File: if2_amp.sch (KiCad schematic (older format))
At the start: 0 parts

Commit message: if2_amp updated
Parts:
- added R? (x2): R, symbol Device:R
- added R? (x2): 100k, symbol Device:R
- added U?: MCP6D11, Package_SO:MSOP-8_3x3mm_P0.65mm, symbol sdr:MCP6D11
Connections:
- new net +5VA: R?.1, U?.3 (V+), U?.7 (/PD)
- new net 2.5V: R?.1, R?.2, U?.2 (Vocm)
- new net GND: R?.2, U?.6 (V-)
- new net In+: R?.2, U?.8 (+)
- new net In-: R?.2, U?.1 (-)
- new net Out+: R?.1, U?.4 (Out+)
- new net Out-: R?.1, U?.5 (Out-)
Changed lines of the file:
@@
 $Descr A4 11693 8268
 encoding utf-8
-Sheet 8 7
+Sheet 6 7
 Title ""
 Date ""
@@
 Comment4 ""
 $EndDescr
+$Comp
+L sdr:MCP6D11 U?
+U 1 1 5FEA4D4E
+P 2450 3150
+F 0 "U?" H 2400 4250 50  0000 C CNN
+F 1 "MCP6D11" H 2400 4150 50  0000 C CNN
+F 2 "Package_SO:MSOP-8_3x3mm_P0.65mm" H 2400 3000 50  0001 L CNN
+F 3 "http://www.ti.com/lit/ds/symlink/opa333.pdf" H 2850 3300 50  0001 C CNN
+	1    2450 3150
+	1    0    0    -1
+$EndComp
+Text HLabel 1800 3050 0    50   Input ~ 0
+In+
+Text HLabel 1800 3250 0    50   Input ~ 0
+In-
+Wire Wire Line
+	1800 3050 2050 3050
+Wire Wire Line
+	1800 3250 2050 3250
+Wire Wire Line
+	2500 2850 2400 2850
+$Comp
+L power:GND #PWR?
+U 1 1 5FEAC1C0
+P 2400 3450
+F 0 "#PWR?" H 2400 3200 50  0001 C CNN
+F 1 "GND" H 2400 3300 50  0000 C CNN
+F 2 "" H 2400 3450 50  0001 C CNN
+F 3 "" H 2400 3450 50  0001 C CNN
+	1    2400 3450
+	1    0    0    -1
+$EndComp
+$Comp
+L Device:R R?
+U 1 1 5FEAD645
+P 2400 2450
+F 0 "R?" V 2193 2450 50  0000 C CNN
+F 1 "R" V 2284 2450 50  0000 C CNN
+F 2 "" V 2330 2450 50  0001 C CNN
+F 3 "~" H 2400 2450 50  0001 C CNN
+	1    2400 2450
+	0    1    1    0
+$EndComp
+$Comp
+L Device:R R?
+U 1 1 5FEAE12B
+P 2400 3850
+F 0 "R?" V 2600 3850 50  0000 C CNN
+F 1 "R" V 2500 3850 50  0000 C CNN
+F 2 "" V 2330 3850 50  0001 C CNN
+F 3 "~" H 2400 3850 50  0001 C CNN
+	1    2400 3850
+	0    1    1    0
+$EndComp
+Wire Wire Line
+	2250 2450 2050 2450
+Wire Wire Line
+	2050 2450 2050 3050
+Connection ~ 2050 3050
+Wire Wire Line
+	2050 3050 2150 3050
+Wire Wire Line
+	2050 3250 2050 3850
+Wire Wire Line
+	2050 3850 2250 3850
+Connection ~ 2050 3250
+Wire Wire Line
+	2050 3250 2150 3250
+Wire Wire Line
+	2550 3850 2800 3850
+Wire Wire Line
+	2800 3850 2800 3250
+Wire Wire Line
+	2800 3050 2800 2450
+Wire Wire Line
+	2800 2450 2550 2450
+Text HLabel 3150 3050 2    50   Input ~ 0
+Out+
+Text HLabel 3150 3250 2    50   Input ~ 0
+Out-
+Wire Wire Line
+	3150 3050 2800 3050
+Connection ~ 2800 3050
+Wire Wire Line
+	2800 3250 3150 3250
+Connection ~ 2800 3250
+Wire Wire Line
+	2800 3150 2750 3150
+$Comp
+L power:+5VA #PWR?
+U 1 1 5FEB0DF4
+P 2400 2850
+F 0 "#PWR?" H 2400 2700 50  0001 C CNN
+F 1 "+5VA" H 2415 3023 50  0000 C CNN
+F 2 "" H 2400 2850 50  0001 C CNN
+F 3 "" H 2400 2850 50  0001 C CNN
+	1    2400 2850
+	1    0    0    -1
+$EndComp
+Connection ~ 2400 2850
+$Comp
+L power:+5VA #PWR?
+U 1 1 5FEB1889
+P 4000 2200
+F 0 "#PWR?" H 4000 2050 50  0001 C CNN
+F 1 "+5VA" H 4015 2373 50  0000 C CNN
+F 2 "" H 4000 2200 50  0001 C CNN
+F 3 "" H 4000 2200 50  0001 C CNN
+	1    4000 2200
+	1    0    0    -1
+$EndComp
+$Comp
+L Device:R R?
+U 1 1 5FEB1EAA
+P 4000 2350
+F 0 "R?" H 4070 2396 50  0000 L CNN
+F 1 "100k" H 4070 2305 50  0000 L CNN
+F 2 "" V 3930 2350 50  0001 C CNN
+F 3 "~" H 4000 2350 50  0001 C CNN
+	1    4000 2350
+	1    0    0    -1
+$EndComp
+$Comp
+L Device:R R?
+U 1 1 5FEB22B7
+P 4000 2750
+F 0 "R?" H 4070 2796 50  0000 L CNN
+F 1 "100k" H 4070 2705 50  0000 L CNN
+F 2 "" V 3930 2750 50  0001 C CNN
+F 3 "~" H 4000 2750 50  0001 C CNN
+	1    4000 2750
+	1    0    0    -1
+$EndComp
+$Comp
+L power:GND #PWR?
+U 1 1 5FEB26F6
+P 4000 2900
+F 0 "#PWR?" H 4000 2650 50  0001 C CNN
+F 1 "GND" H 4000 2750 50  0000 C CNN
+F 2 "" H 4000 2900 50  0001 C CNN
+F 3 "" H 4000 2900 50  0001 C CNN
+	1    4000 2900
+	1    0    0    -1
+$EndComp
+Text GLabel 2800 3150 2    50   Input ~ 0
+2.5V
+Text GLabel 4050 2550 2    50   Input ~ 0
+2.5V
+Wire Wire Line
+	4000 2500 4000 2550
+Wire Wire Line
+	4000 2550 4050 2550
+Connection ~ 4000 2550
+Wire Wire Line
+	4000 2550 4000 2600
 $EndSCHEMATC

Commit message: if2 completed
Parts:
- R? (x2): value R -> 10k
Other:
- note added: "If we want to compensate for the previous filter's attenuation, we need a 26k resistor in order to have in total 30.8 dB gain\n"
- note added: "The previous filter has 750 ohm output impedance\n"
- note added: "This way, we have exactly 22dB\n"
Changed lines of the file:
@@
 P 2400 2450
 F 0 "R?" V 2193 2450 50  0000 C CNN
-F 1 "R" V 2284 2450 50  0000 C CNN
+F 1 "10k" V 2284 2450 50  0000 C CNN
 F 2 "" V 2330 2450 50  0001 C CNN
 F 3 "~" H 2400 2450 50  0001 C CNN
@@
 P 2400 3850
 F 0 "R?" V 2600 3850 50  0000 C CNN
-F 1 "R" V 2500 3850 50  0000 C CNN
+F 1 "10k" V 2500 3850 50  0000 C CNN
 F 2 "" V 2330 3850 50  0001 C CNN
 F 3 "~" H 2400 3850 50  0001 C CNN
@@
 Wire Wire Line
 	4000 2550 4000 2600
+Text Notes 1250 1350 0    50   ~ 0
+If we want to compensate for the previous filter's attenuation, we need a 26k resistor in order to have in total 30.8 dB gain\n
+Text Notes 1250 1500 0    50   ~ 0
+This way, we have exactly 22dB\n
+Text Notes 1250 1650 0    50   ~ 0
+The previous filter has 750 ohm output impedance\n
 $EndSCHEMATC

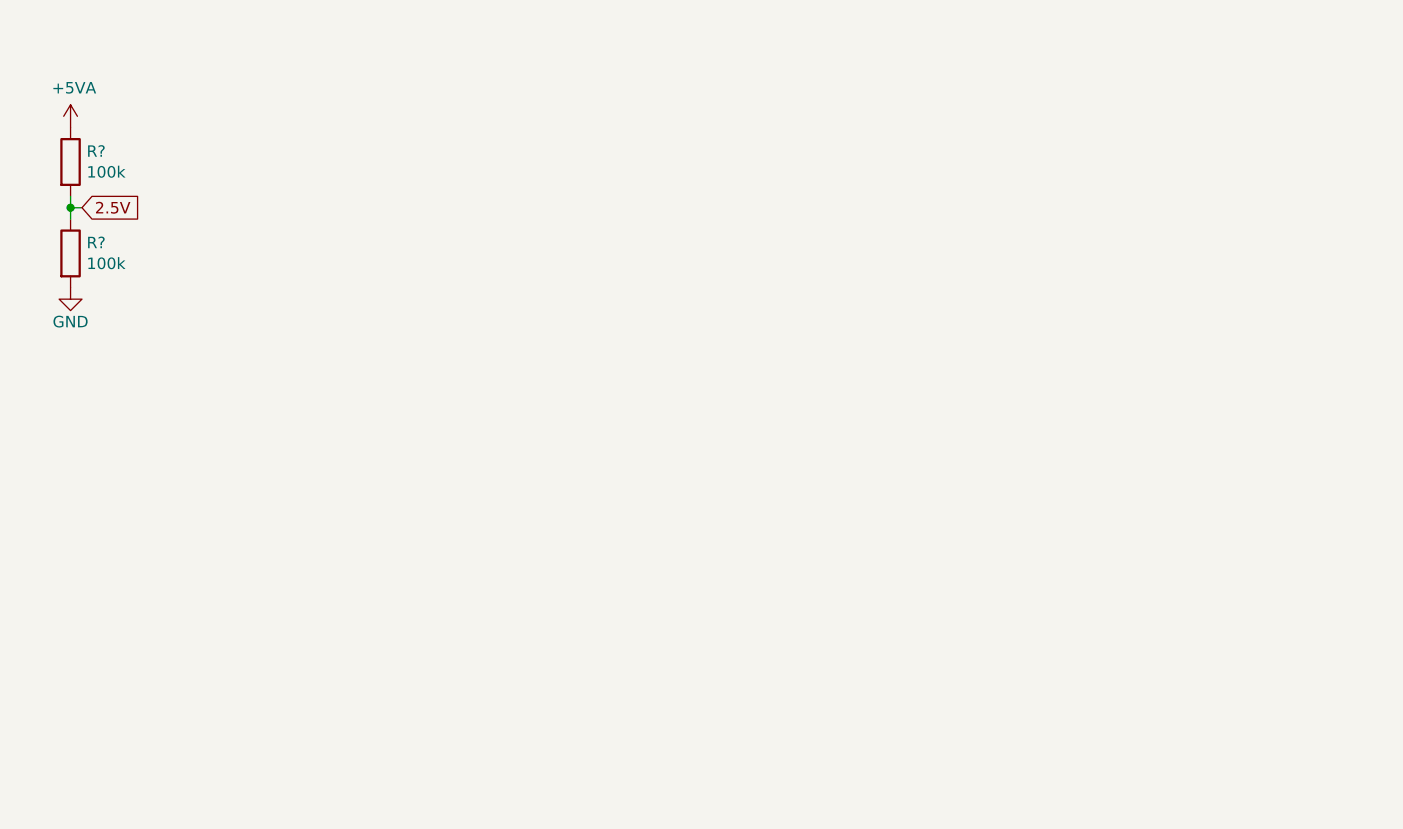
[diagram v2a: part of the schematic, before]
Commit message: IF2 amp discrete demo
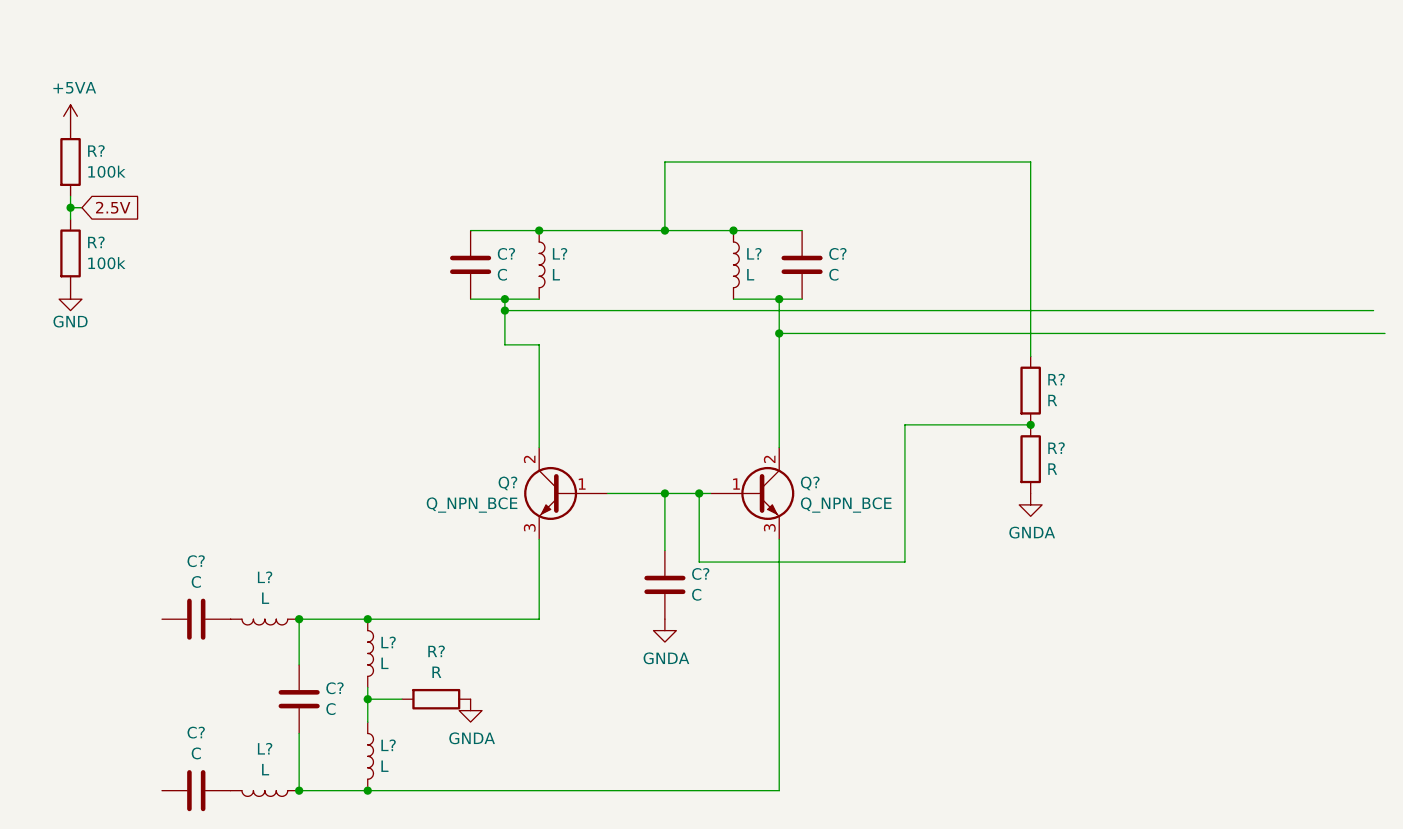
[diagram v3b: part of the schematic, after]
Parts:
- added C? (x6): C, symbol Device:C
- added L? (x6): L, symbol Device:L
- added Q? (x2): Q_NPN_BCE, symbol Device:Q_NPN_BCE
- added R? (x3): R, symbol Device:R
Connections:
- net labels added: GNDA
- wire segments 19 -> 57

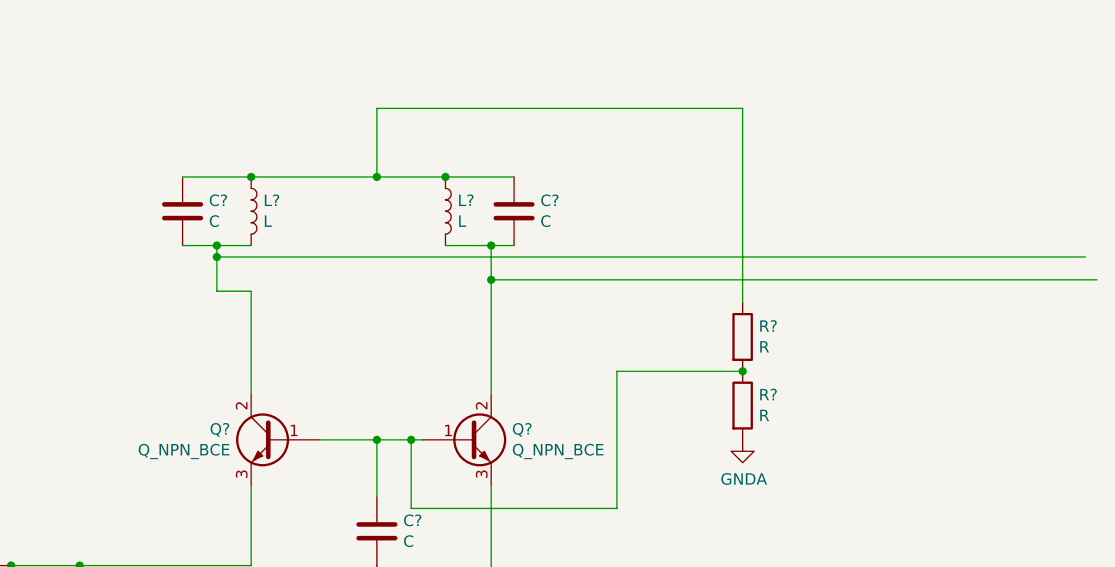
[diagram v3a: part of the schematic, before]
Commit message: IF2 AMP modified collector tank
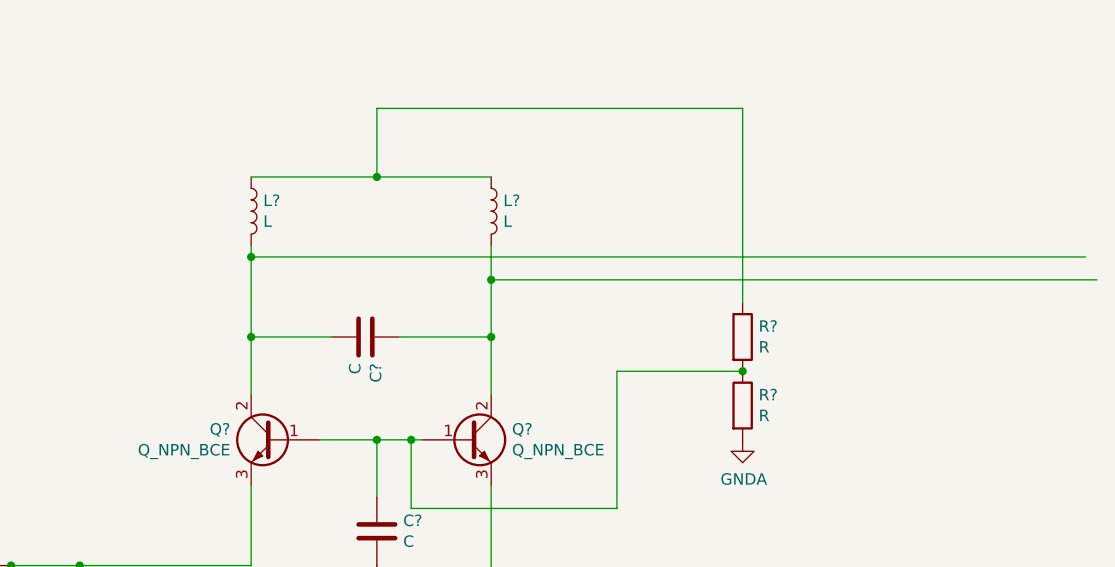
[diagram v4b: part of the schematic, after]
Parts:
- removed C?: C, symbol Device:C
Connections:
- wire segments 57 -> 53
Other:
- moved on the sheet: C?, L?
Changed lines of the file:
@@
 L Device:C C?
 U 1 1 5FEC7CF1
-P 5750 2800
-F 0 "C?" H 5865 2846 50  0000 L CNN
-F 1 "C" H 5865 2755 50  0000 L CNN
-F 2 "" H 5788 2650 50  0001 C CNN
-F 3 "~" H 5750 2800 50  0001 C CNN
-	1    5750 2800
-	1    0    0    -1
+P 6550 3350
+F 0 "C?" H 6665 3396 50  0000 L CNN
+F 1 "C" H 6665 3305 50  0000 L CNN
+F 2 "" H 6588 3200 50  0001 C CNN
+F 3 "~" H 6550 3350 50  0001 C CNN
+	1    6550 3350
+	0    1    1    0
 $EndComp
 $Comp
 L Device:L L?
 U 1 1 5FEC838F
-P 6900 2800
-F 0 "L?" H 6953 2846 50  0000 L CNN
-F 1 "L" H 6953 2755 50  0000 L CNN
-F 2 "" H 6900 2800 50  0001 C CNN
-F 3 "~" H 6900 2800 50  0001 C CNN
-	1    6900 2800
-	1    0    0    -1
-$EndComp
-$Comp
-L Device:C C?
-U 1 1 5FEC8B7D
-P 7200 2800
-F 0 "C?" H 7315 2846 50  0000 L CNN
-F 1 "C" H 7315 2755 50  0000 L CNN
-F 2 "" H 7238 2650 50  0001 C CNN
-F 3 "~" H 7200 2800 50  0001 C CNN
-	1    7200 2800
+P 7100 2800
+F 0 "L?" H 7153 2846 50  0000 L CNN
+F 1 "L" H 7153 2755 50  0000 L CNN
+F 2 "" H 7100 2800 50  0001 C CNN
+F 3 "~" H 7100 2800 50  0001 C CNN
+	1    7100 2800
 	1    0    0    -1
 $EndComp
 Wire Wire Line
-	7100 3600 7100 3100
-Wire Wire Line
-	7100 2950 6900 2950
-Wire Wire Line
-	7200 2950 7100 2950
-Connection ~ 7100 2950
-Wire Wire Line
-	5750 2950 5900 2950
-Wire Wire Line
-	6050 3600 6050 3150
-Wire Wire Line
-	6050 3150 5900 3150
-Wire Wire Line
-	5900 3150 5900 3000
-Connection ~ 5900 2950
-Wire Wire Line
-	5900 2950 6050 2950
-Wire Wire Line
-	5750 2650 6050 2650
-Connection ~ 6050 2650
-Wire Wire Line
 	6050 2650 6600 2650
-Connection ~ 6900 2650
-Wire Wire Line
-	6900 2650 7200 2650
 Wire Wire Line
 	8200 3200 8200 2350
@@
 Connection ~ 6600 2650
 Wire Wire Line
-	6600 2650 6900 2650
+	6600 2650 7100 2650
 Wire Wire Line
 	7100 3100 9750 3100
@@
 	7100 3100 7100 2950
 Wire Wire Line
-	5900 3000 9700 3000
-Connection ~ 5900 3000
+	6050 3000 9700 3000
+Connection ~ 6050 3000
 Wire Wire Line
-	5900 3000 5900 2950
+	6050 3000 6050 2950
+Wire Wire Line
+	6050 3000 6050 3350
+Wire Wire Line
+	6700 3350 7100 3350
+Wire Wire Line
+	7100 3100 7100 3350
+Connection ~ 7100 3350
+Wire Wire Line
+	7100 3350 7100 3600
+Wire Wire Line
+	6400 3350 6050 3350
+Connection ~ 6050 3350
+Wire Wire Line
+	6050 3350 6050 3600
 $EndSCHEMATC

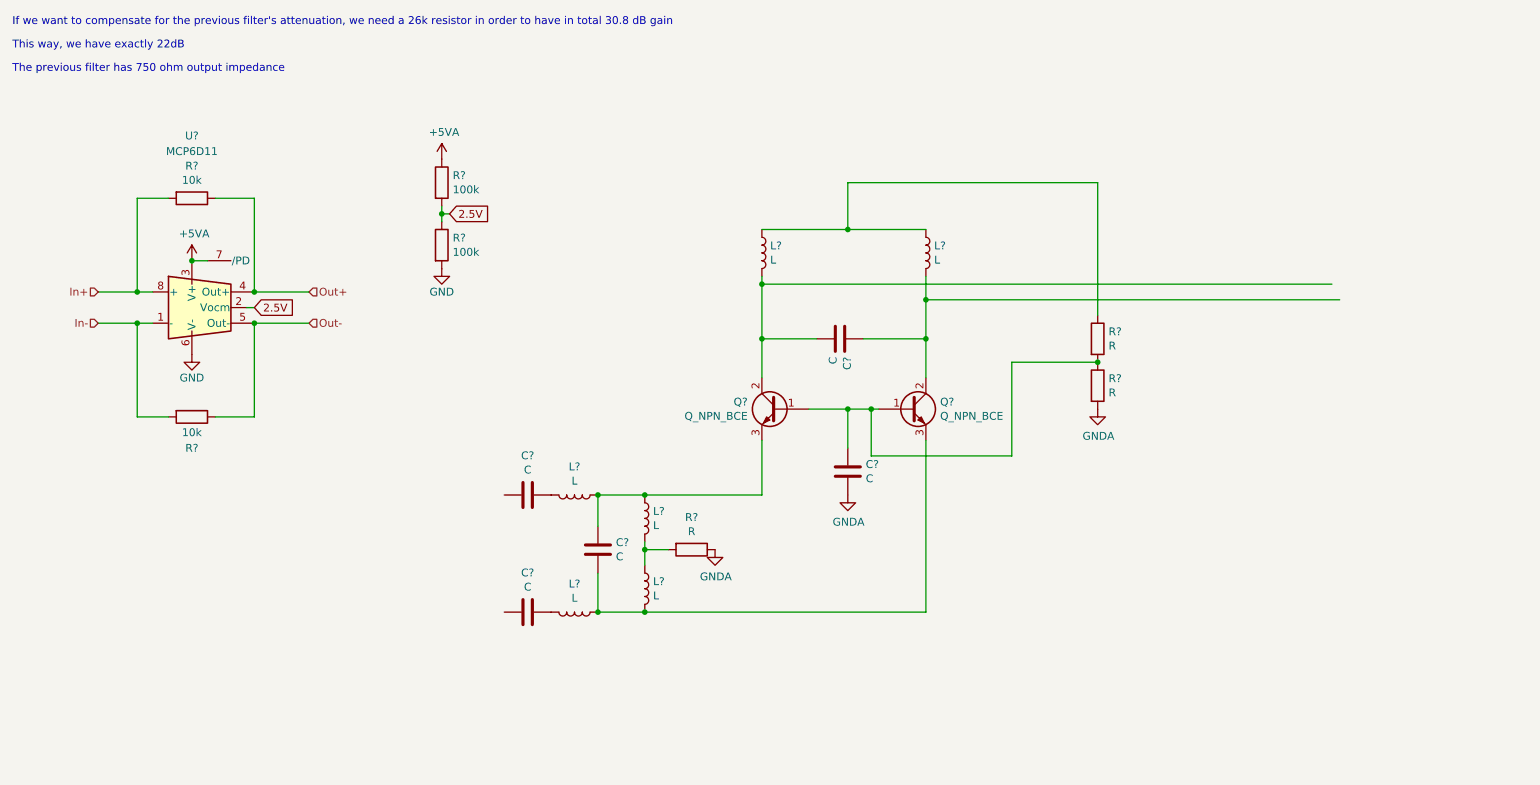
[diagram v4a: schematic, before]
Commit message: If2 50 ohm filter
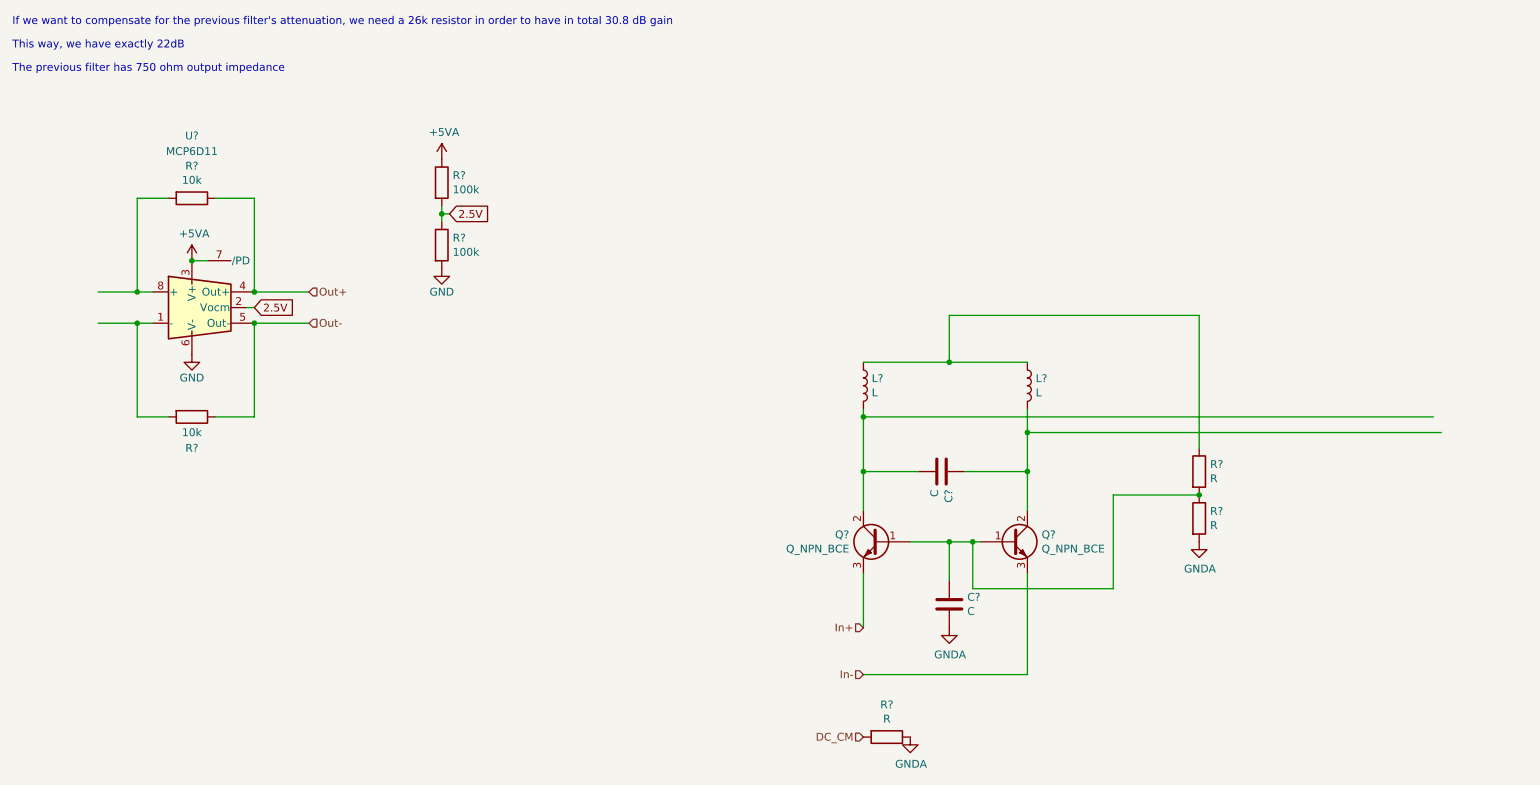
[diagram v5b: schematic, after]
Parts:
- removed C? (x3): C, symbol Device:C
- removed L? (x4): L, symbol Device:L
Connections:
- net labels added: DC_CM
- wire segments 53 -> 45
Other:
- moved on the sheet: C?, L?, Q?, R?
